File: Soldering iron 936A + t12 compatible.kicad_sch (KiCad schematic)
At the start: 109 parts, among them J1 DC INPUT, J2 USB TO SERIAL, J3 AC input, J4 output_connector, J5 mosfet_driver_future_backup, J6 OLED, J7 USB C BREAKOUT BOARD, Q1 IRF9540N, Q2 BC547, SW1 RotaryEncoder_Switch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

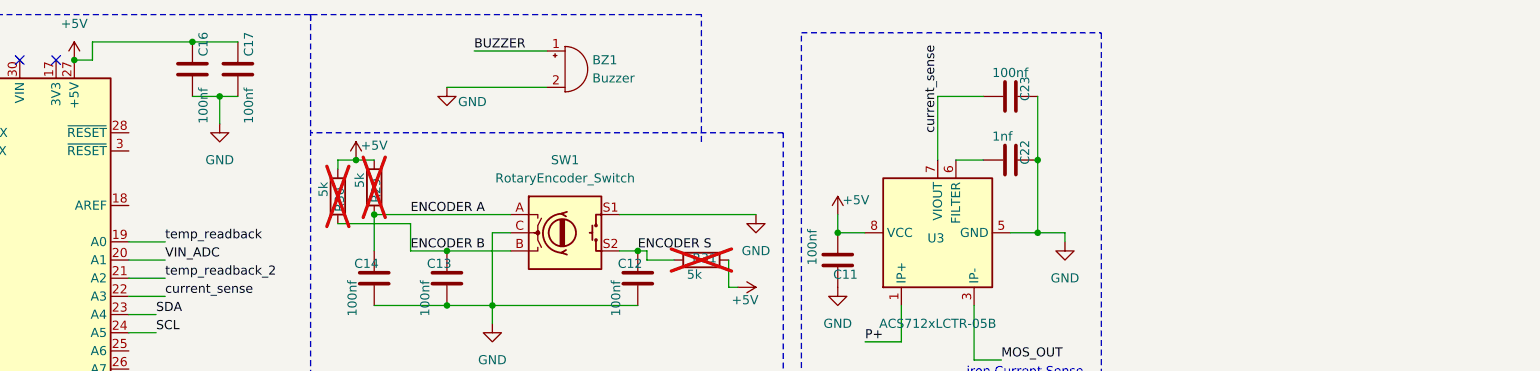
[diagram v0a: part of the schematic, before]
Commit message: Added , placed refernce , next have to check warnings , silkscreen
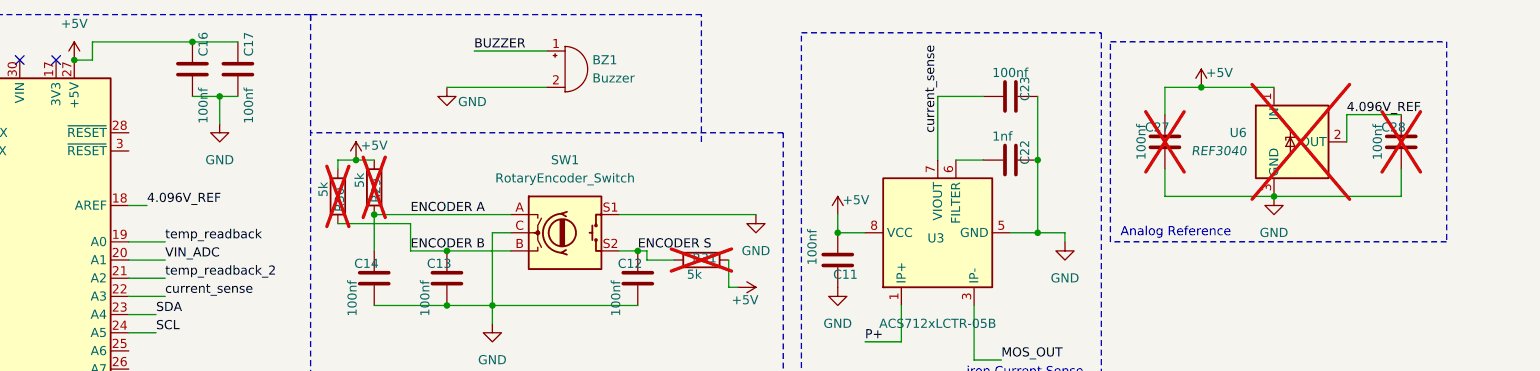
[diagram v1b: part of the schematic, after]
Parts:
- added C27, C28: 100nf, Capacitor_SMD:C_0603_1608Metric_Pad1.08x0.95mm_HandSolder, symbol Device:C
- added U6: REF3040, Package_TO_SOT_SMD:SOT-23, symbol Reference_Voltage:REF3040
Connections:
- net +5V: now also C27.1, U6.1 (IN)
- net GND: now also C27.2, C28.2, U6.3 (GND)
- net 4.096V_REF: now reaches A1.18 (AREF)
- net 4.096V_REF: now also C28.1, U6.2 (OUT)
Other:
- note added: "Analog Reference"

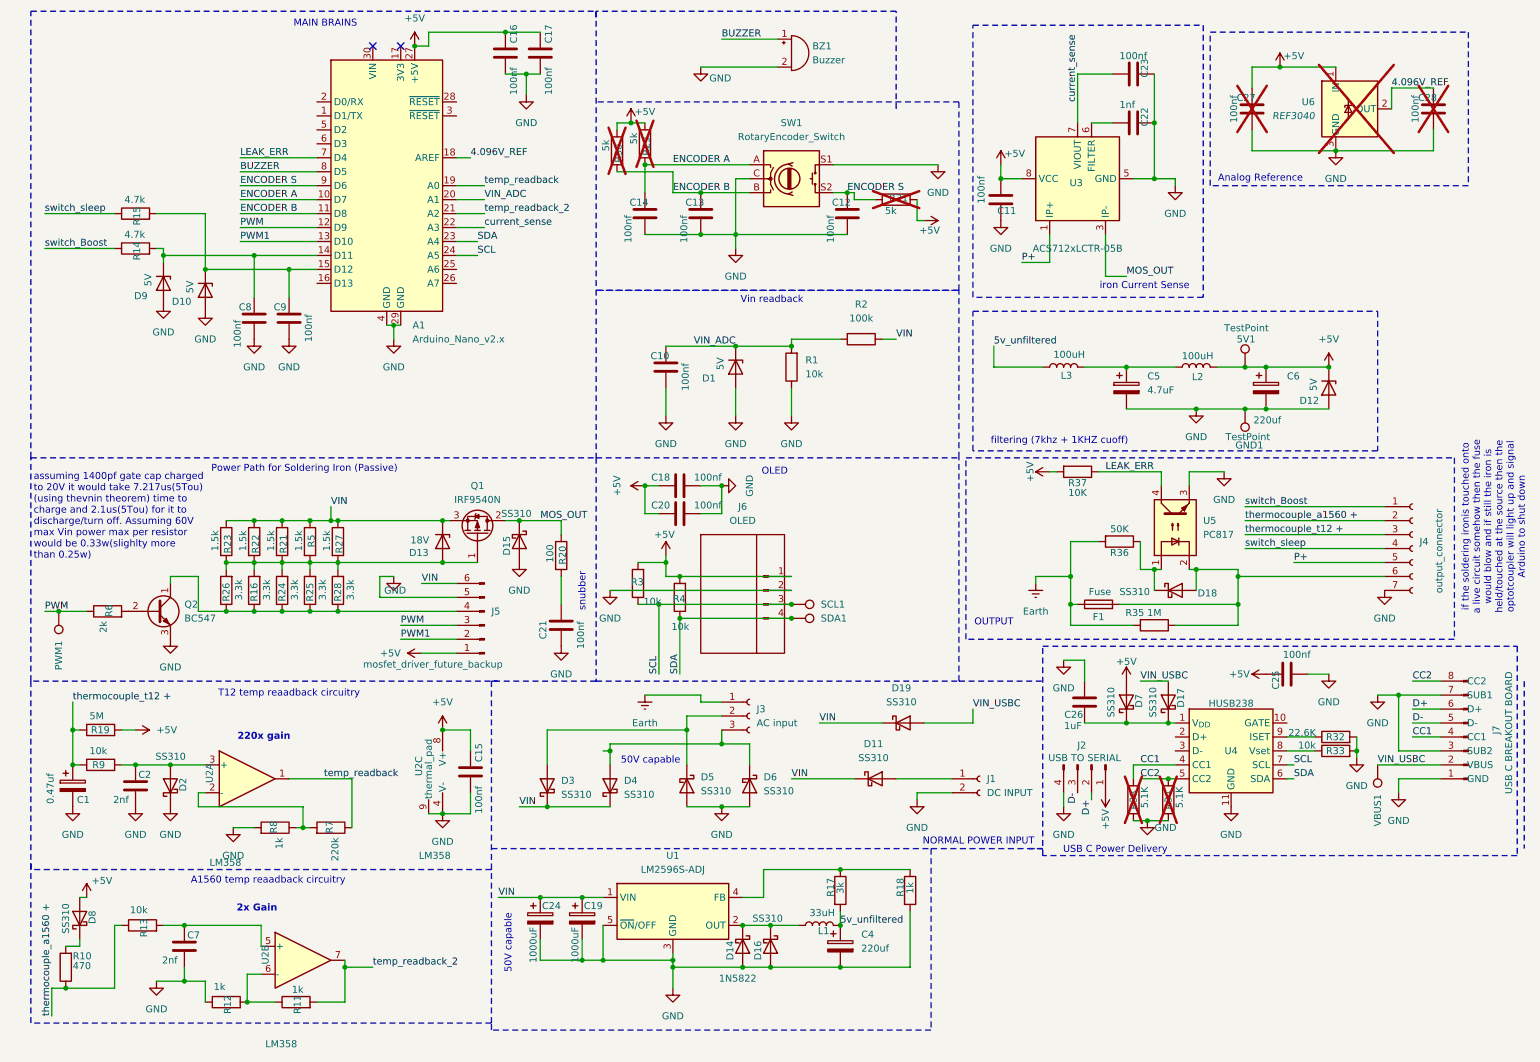
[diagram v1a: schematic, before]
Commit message: added ESD diodes
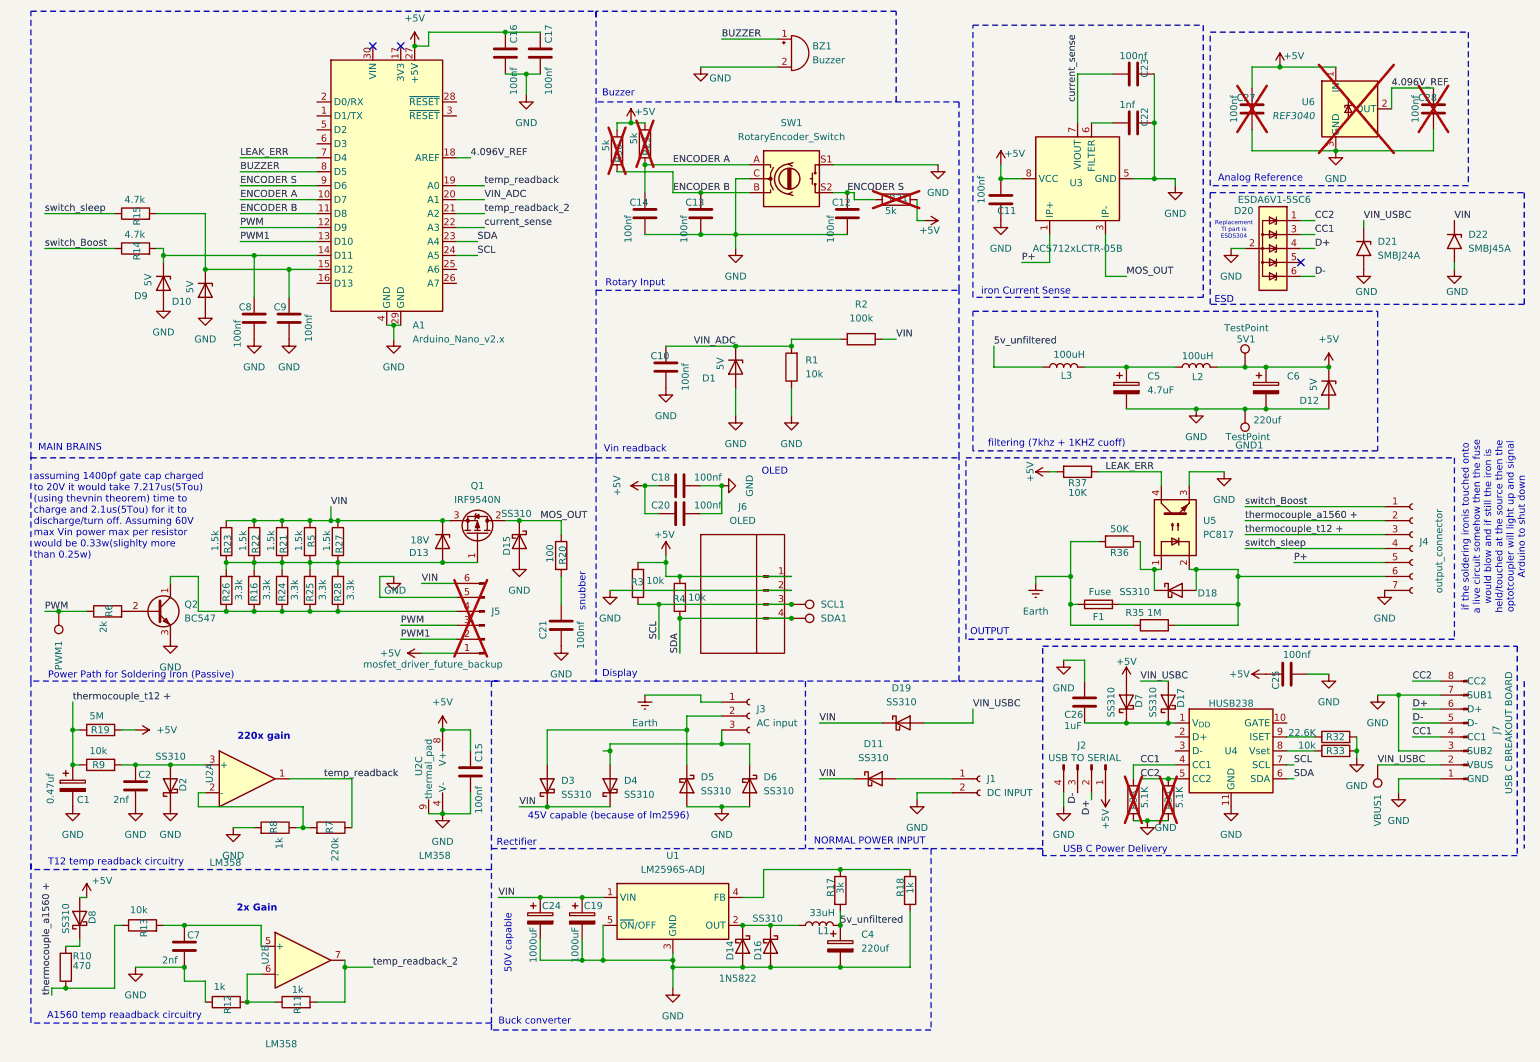
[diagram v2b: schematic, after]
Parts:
- added D20: ESDA6V1-5SC6, Package_TO_SOT_SMD:SOT-23-6, symbol Power_Protection:ESDA6V1-5SC6
- added D21: SMBJ24A, Diode_SMD:D_SMB, symbol Diode:SM6T6V8A
- added D22: SMBJ45A, Diode_SMD:D_SMB, symbol Diode:SM6T6V8A
- J5: now not fitted
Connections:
- net CC1: now also D20.3 (IO2)
- net CC2: now also D20.1 (IO1)
- net D+: now also D20.4 (IO3)
- net D-: now also D20.6 (IO5)
- net GND: now also D20.2 (GND), D21.2 (A2), D22.2 (A2)
- net VIN: now also D22.1 (A1)
- net VIN_USBC: now also D21.1 (A1)
- no-connect marks 2 -> 3
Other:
- note added: "45V capable (because of lm2596)"
- note added: "Buck converter"
- note added: "Buzzer"
- note added: "Display"
- note added: "ESD"
- note added: "Rectifier"
- note added: "Replacement TI part is ESDS304"
- note added: "Rotary Input"
- note added: "T12 temp readback circuitry"
- note removed: "T12 temp reaadback circuitry"

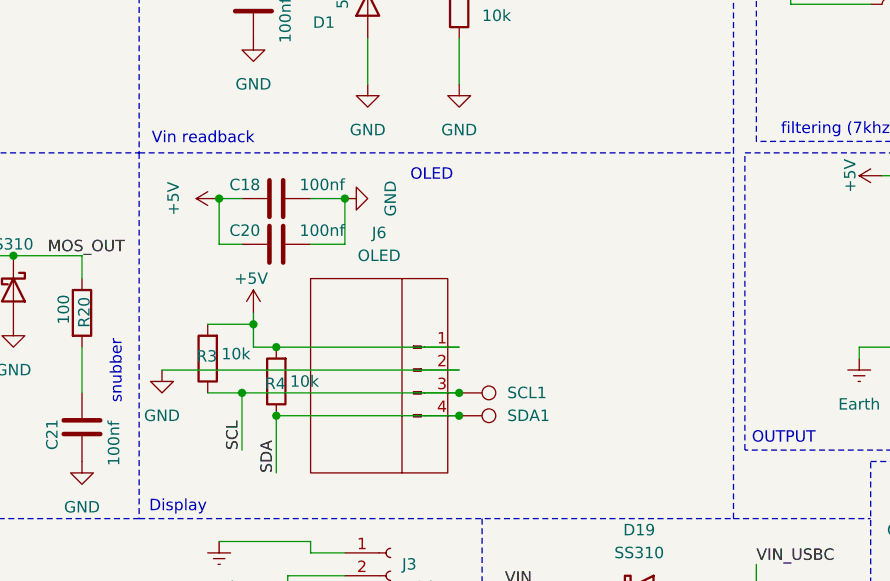
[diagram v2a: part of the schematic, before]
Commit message: added esd , oled support headers , oled switchable pinout
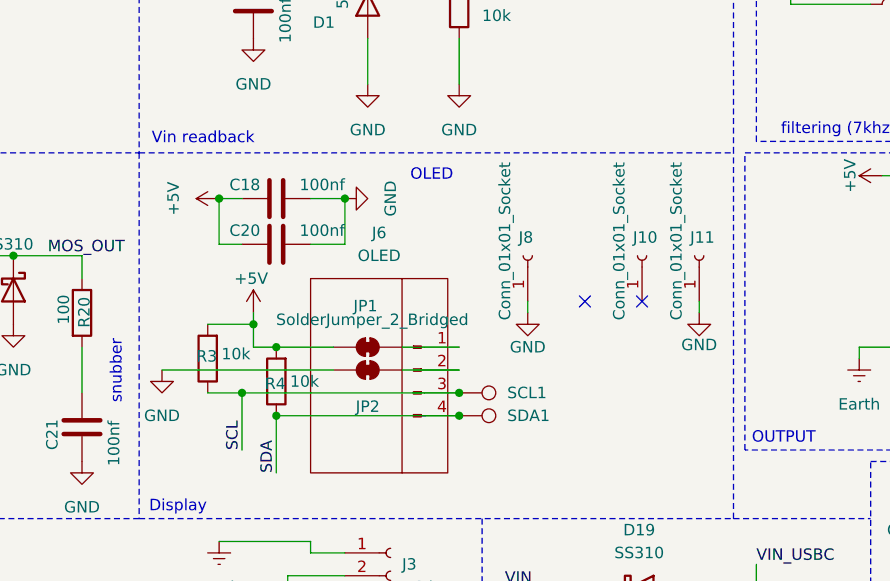
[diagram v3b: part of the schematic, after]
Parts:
- added J10, J11, J8: Conn_01x01_Socket, Connector_PinHeader_2.54mm:PinHeader_1x01_P2.54mm_Vertical, symbol Connector:Conn_01x01_Socket
- added JP1, JP2: SolderJumper_2_Bridged, symbol Jumper:SolderJumper_2_Bridged
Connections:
- net +5V: now also JP1.1 (A); no longer J6.1 (SDA)
- net GND: now also J11.1 (Pin_1), J8.1 (Pin_1), JP2.1 (A); no longer J6.2 (SCL)
- new net: J6.2 (SCL), JP2.2 (B)
- new net: J6.1 (SDA), JP1.2 (B)
- no-connect marks 3 -> 5
